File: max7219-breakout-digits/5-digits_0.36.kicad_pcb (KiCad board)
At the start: 2 copper layers, 53.5 x 15.5 mm, 6 parts, among them J1 Conn_02x08_Odd_Even, U1 HDSM-443B_7-Segment_2_Digit, U2 HDSM-443B_7-Segment_3_Digit

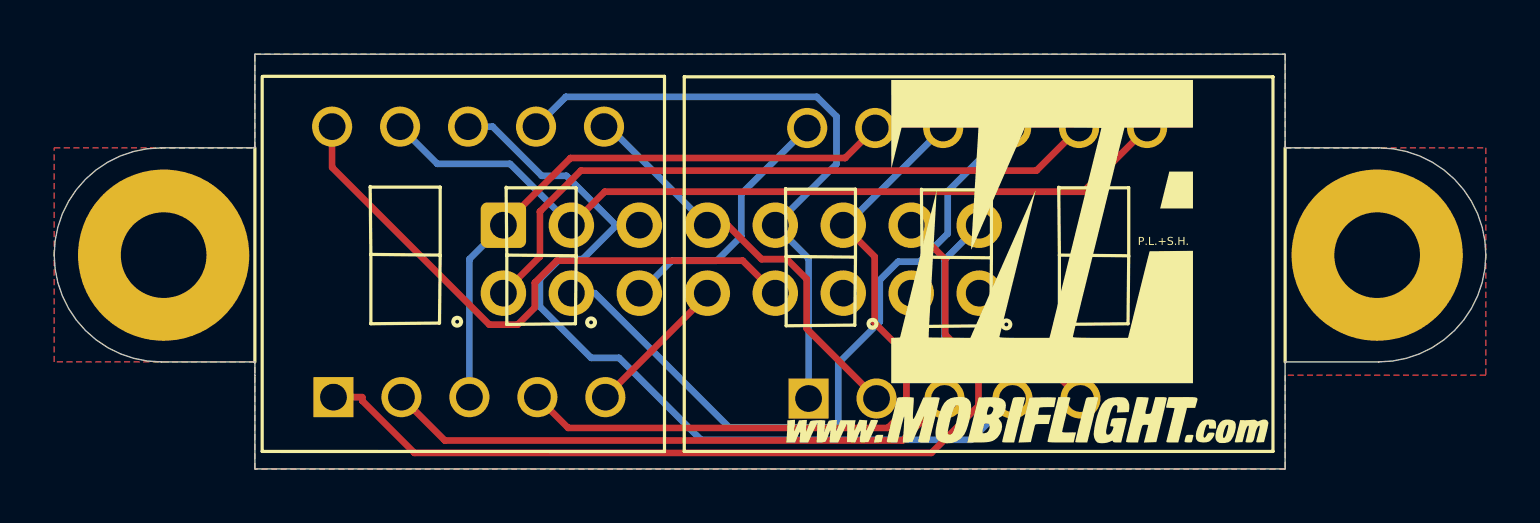
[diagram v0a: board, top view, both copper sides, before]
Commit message: center IDC on all 0.36 display boards
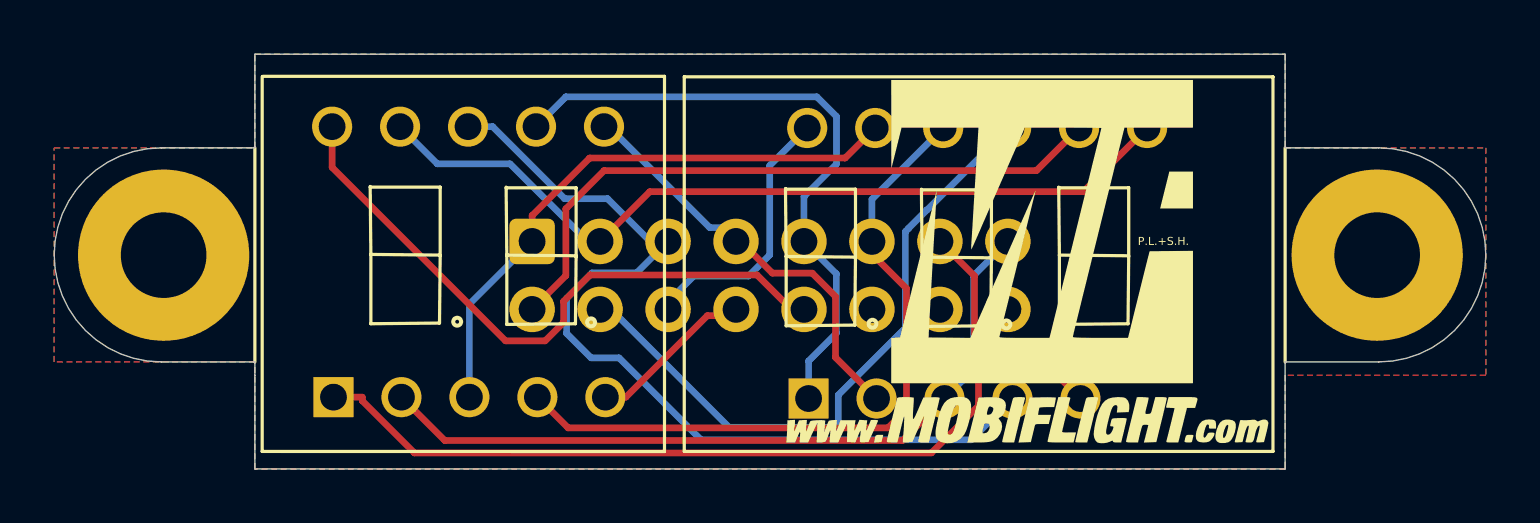
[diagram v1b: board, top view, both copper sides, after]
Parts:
- moved J1 1.23 mm to (100.4, 47.0)
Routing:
- net /DIG4: track 22.6 -> 23.9 mm
- net /DIG1: track 26.3 -> 25.0 mm
- net /C: track 33.0 -> 34.2 mm
- net /G: track 37.9 -> 36.8 mm
- net /F: track 27.7 -> 26.7 mm
- net /DIG3: track 5.46 -> 6.24 mm
- net /D: track 15.5 -> 16.0 mm
- net /B: track 30.9 -> 31.4 mm
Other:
- board text added: "MobiFlight Display System 5 Digits ${REVISION}"
- board text removed: "5 Digit Module ${REVISION}"

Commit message: add additional labels on front on backside from all boards
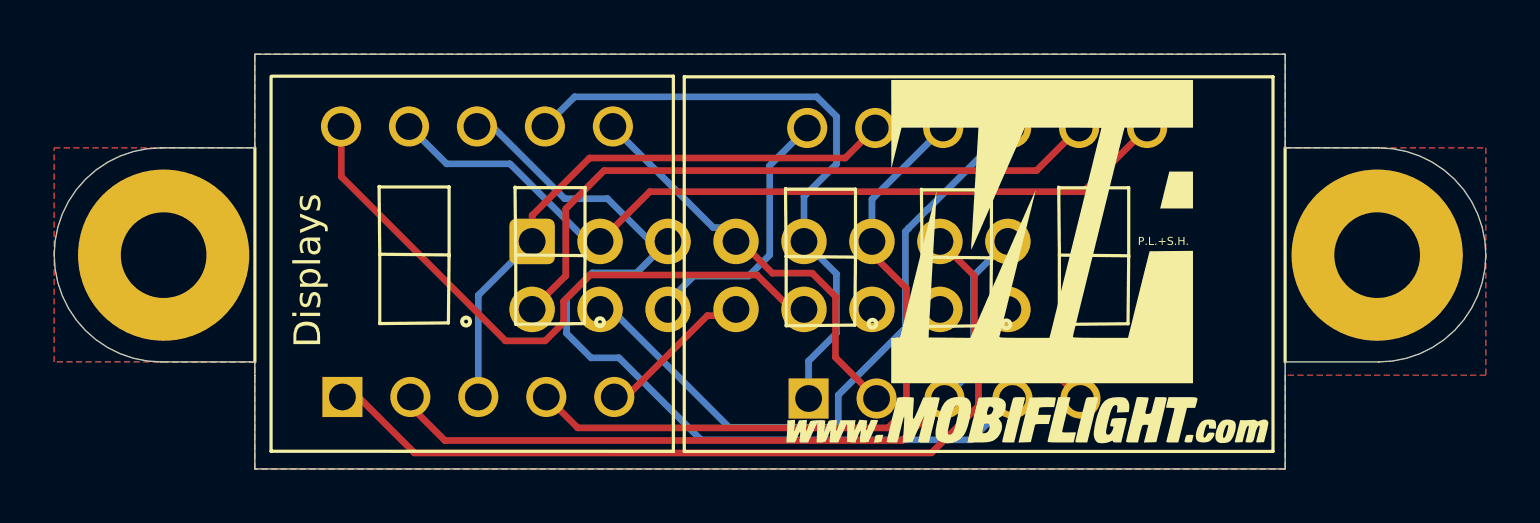
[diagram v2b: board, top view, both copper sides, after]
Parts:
- moved U1 0.33 mm to (102.3, 47.7)
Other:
- board text added: "Displays"
- board text added: "IDC"

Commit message: upadate labels
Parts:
- moved U1 0.23 mm to (102.0, 47.7)

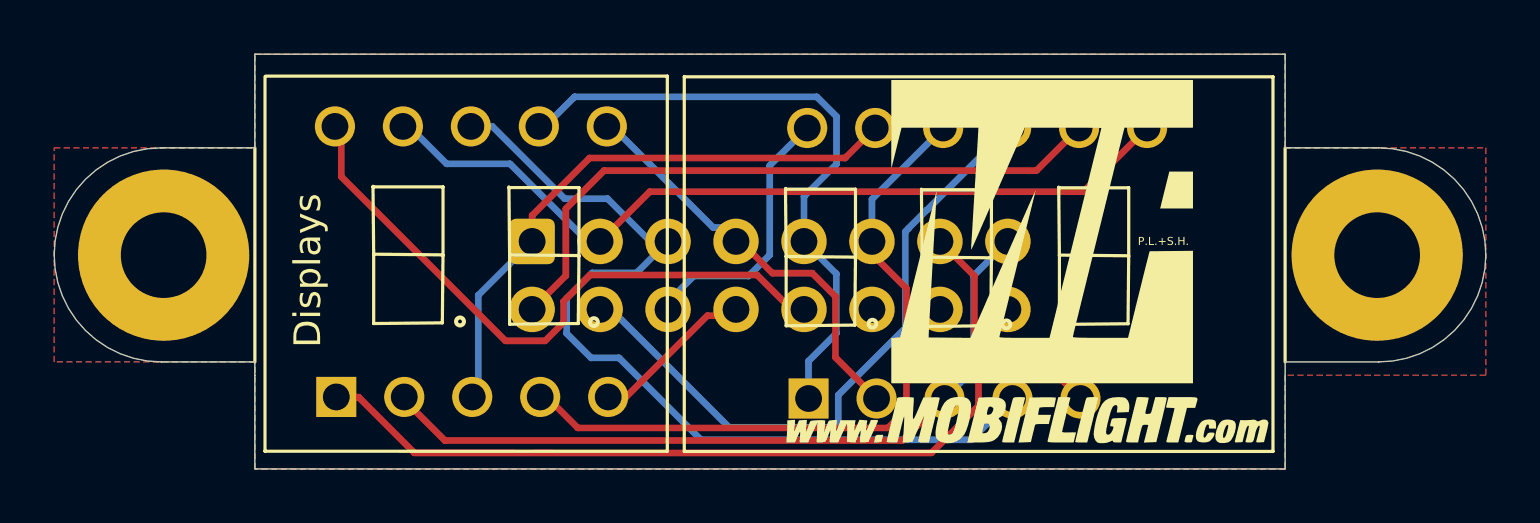
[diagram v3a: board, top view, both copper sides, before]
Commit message: center all IDC connectors on 0.36 boards, move displays closer together
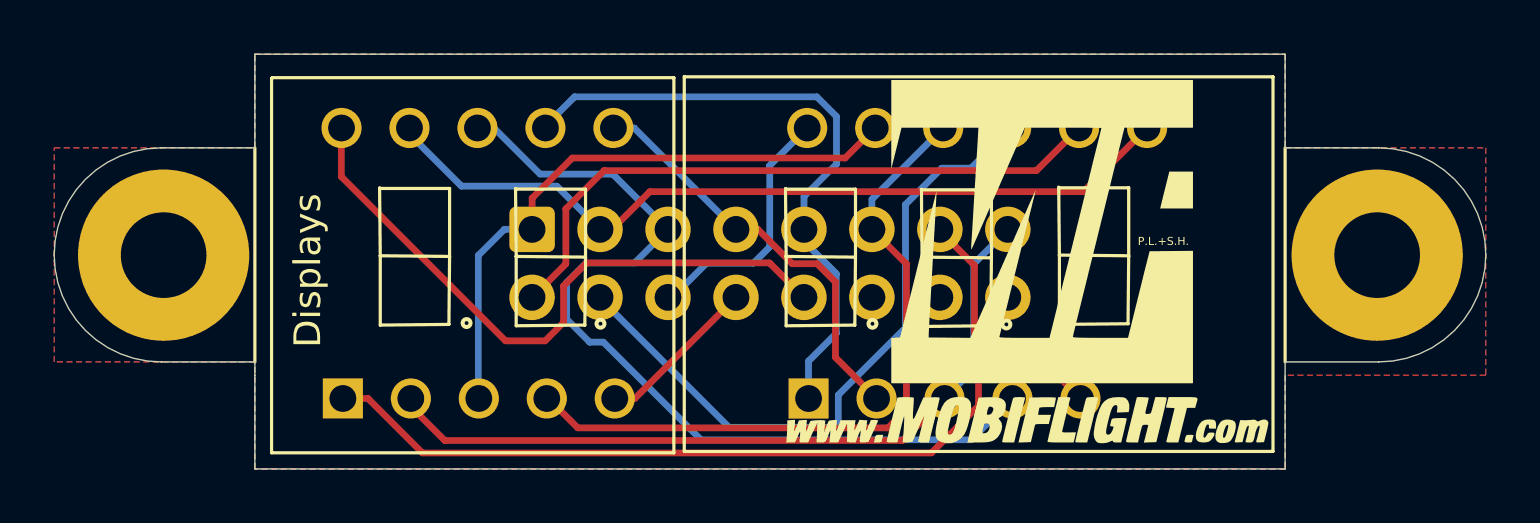
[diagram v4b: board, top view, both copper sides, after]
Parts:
- moved J1 0.45 mm to (100.4, 46.5)
- moved U1 0.25 mm to (102.3, 47.7)
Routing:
- net /A: track 22.1 -> 23.4 mm
- net /D: track 16.0 -> 17.1 mm
- net /DIG4: track 23.8 -> 24.6 mm
- net /DIG1: track 25.0 -> 25.6 mm
- net /DP: track 28.4 -> 29.0 mm
